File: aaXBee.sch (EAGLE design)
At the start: 67 parts, among them Q1 IRLML6244TR, U1 MCP1640C, U2 ATmega328P-AU, U3 DS3232, X1 XB24-Z7WIT-004, Y2 8MHz

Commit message: First reasonably complete routing.
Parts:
- removed C10: 27pF, _jc:C-USM0805
- removed D2: Green, adafruit:LEDCHIPLED_1206
- removed JMP1: solder jumper, _jc:R-US_M0805
- removed JP4: RTC BACKUP, SparkFun:M03LOCK
- removed R8: 1K, _jc:R-US_M0805
- removed S1: RESET, _jc:SPST-NO-MCTACT-6X3.5-SMT
- removed U3: DS3232, _jc:DS323220
- removed X1: XB24-Z7WIT-004, _jc:ULINK_XBEEOVALPADS
- removed Y2: 8MHz, _jc:CRYSTALABM2
- added A1: XB24-Z7WIT-004, _jc:ULINK_XBEEOVALPADS
- added B2: 2xAA, _jc:BATTERY-2AANOHOLES
- added C12, C13: 100nF, _jc:C-USM0805
- added C14, C16: 27pF, _jc:C-USM0805
- added L2: 10uH, _jc:INDUCTORM0805
- added L3: 4.7uH, _jc:INDUCTORNRS4018
- added PR14, PR15, PR16, PR17: PROTO-10, _jc:PROTO-10
- added R16: 562K, _jc:R-US_M0805
- added R17: 249K, _jc:R-US_M0805
- added SJ1: 5V, jumper:SJ
- added SJ2: (no value), jumper:SJ2W
- added SJ3: 3V3, jumper:SJ
- added SW1: (no value), _jc:SPST-NO-MCTACT-6X3.5-SMT
- added SW2: RESET, _jc:SPST-NO-MCTACT-6X3.5-SMT
- added U4: ATmega328P-AU, atmel:MEGA8-AI
- added U5: MCP9808, _jc:MCP9808
- added U6: DS3231, _jc:DS3231
- added Y1: 8MHz, _jc:CRYSTALABM2
- C15: value 10uF -> 100nF; device _jc:C-USC0805 -> _jc:C-USM0805
- C6, C7: value 100nF -> 10uF
- C9: value 27pF -> 100nF
- D1: value Red -> Yellow; device adafruit:LEDCHIPLED_1206 -> _jc:LEDD0805
- D7, D8: device adafruit:LEDCHIPLED_0805 -> _jc:LEDD0805
- R13, R14, R15: device _jc:R-US_R0805 -> _jc:R-US_M0805
- R3: value 249K -> 976K
- U1: value MCP1640C -> MCP1640D
- U2: value ATmega328P-AU -> MCP1640D; device atmel:MEGA8-AI -> _jc:MCP1640
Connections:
- removed net LED2: R8.2, U2.PB0(ICP)
- removed net N$11: C10.1, U2.PB7(XTAL2/TOSC2), Y2.1
- removed net N$3: D2.A, R8.1
- removed net N$39: R14.2, X1.PWM0/RSSI
- removed net N$40: R15.2, X1.ASC/AD5/DIO5
- new net AREF: C13.1, JP1.1, U4.AREF
- new net ASC: A1.ASC/AD5/DIO5, R15.2
- new net CTS: A1.CTS/DIO7, U4.PD5(T1)
- new net N$43: C14.1, U4.PB6(XTAL1/TOSC1), Y1.2
- new net N$44: C16.1, U4.PB7(XTAL2/TOSC2), Y1.1
- new net N$46: C12.1, L2.2, U4.AVCC
- new net RSSI: A1.PWM0/RSSI, R14.2
- new net SLP: A1.DTR/DI8, U4.PD6(AIN0)
- new net SW1: SW1.P$1, U4.PB0(ICP)
- net +3V3: now also C7.1, R3.1, SJ2.1, U2.VOUT; no longer C15.1, R13.1, X1.+3V3
- net /RESET: now also SW2.P$1, U4.PC6(/RESET); no longer S1.P$1, U2.PC6(/RESET)
- net /SS: now also JP1.12, U4.PB2(SS/OC1B); no longer JP1.9, U2.PB2(SS/OC1B)
- net 32KHZ: now also U6.32KHZ; no longer JP1.1, U3.32KHZ
- net ADC0: now also U4.PC0(ADC0); no longer U2.PC0(ADC0)
- net ADC1: now also U4.PC1(ADC1); no longer U2.PC1(ADC1)
- net ADC2: now also U4.PC2(ADC2); no longer U2.PC2(ADC2)
- net ADC3: now also U4.PC3(ADC3); no longer U2.PC3(ADC3)
- net ADC6: now also U4.ADC6; no longer U2.ADC6
- net ADC7: now also U4.ADC7; no longer U2.ADC7
- net BAT: now also B2.POS, C6.1, L3.1, U2.VIN; no longer JP4.1
- net EN: now also U2.EN, U4.PD4(XCK/T0); no longer U2.PD4(XCK/T0)
- net GND: now also A1.GND, B2.NEG, C12.2, C13.2, C14.2, C16.2, R16.2, R17.2, SJ1.2, SW1.P$2, SW2.P$2, U4.GND, U4.GND@1, U4.GND@2, U5.A0, U5.A1, U5.A2, U5.GND, U6.GND, U6.NC10, U6.NC11, U6.NC12, U6.NC5, U6.NC6, U6.NC7, U6.NC8, U6.NC9; no longer C10.2, D2.C, JMP1.2, R3.2, S1.P$2, U2.GND@1, U2.GND@2, U3.GND, U3.NC1, U3.NC10, U3.NC11, U3.NC12, U3.NC13, U3.NC14, U3.NC19, U3.NC2, U3.NC7, U3.NC8, U3.NC9, X1.GND
- net INT: now also U4.PD3(INT1), U6./INT-SQW; no longer U2.PD3(INT1), U3./INT-SQW
- net LED1: now also U4.PD7(AIN1); no longer U2.PD7(AIN1)
- net MISO: now also JP1.10, U4.PB4(MISO); no longer JP1.11, U2.PB4(MISO)
- net MOSI: now also JP1.11, U4.PB3(MOSI/OC2); no longer JP1.12, U2.PB3(MOSI/OC2)
- net N$1: now also U6.VBAT; no longer JP4.3
- net N$12: now also R16.1, R3.2, U2.VFB; no longer JMP1.1, R2.2, R3.1
- net N$13: now also L3.2, U2.SW; no longer C8.1, U2.AREF
- net N$35: now also A1.+3V3, C15.1, C3.1, R13.1, SJ2.2; no longer JP4.2, U3.VBAT
- net N$37: now also A1.DIN, SJ3.1; no longer X1.DIN
- net N$38: now also A1.DOUT; no longer X1.DOUT
- net N$8: now also R17.1, R2.2, SJ1.1; no longer C9.1, U2.PB6(XTAL1/TOSC1), Y2.2
- net PPWR: now also C9.1, U4.PD2(INT0), U5.VCC, U6.VCC; no longer U2.PD2(INT0), U3.VCC
- net RXD: now also U4.PD0(RXD); no longer U2.PD0(RXD)
- net SCK: now also JP1.9, U4.PB5(SCK); no longer JP1.10, U2.PB5(SCK)
- net SCL: now also R10.2, U4.PC5(ADC5/SCL), U5.SCL, U6.SCL; no longer R10.1, U2.PC5(ADC5/SCL), U3.SCL18
- net SDA: now also R9.2, U4.PC4(ADC4/SDA), U5.SDA, U6.SDA; no longer R9.1, U2.PC4(ADC4/SDA), U3.SDA
- net SPWR: now also U4.PB1(OC1A); no longer U2.PB1(OC1A)
- net TXD: now also SJ3.2, U4.PD1(TXD); no longer U2.PD1(TXD)
- net VCC: now also C8.1, L2.1, R10.1, R9.1, SJ2.3, U4.VCC@1, U4.VCC@2; no longer C3.1, C6.1, C7.1, R10.2, R9.2, U2.AVCC, U2.VCC@1, U2.VCC@2
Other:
- note added: "*Verify XBee connections!"
- note added: "Double-A XBee Sensor Node by Jack Christensen is licensed under"
- note added: "Main 5V or 3.3V supply"
- note added: "XBee 3.3V supply"
- note removed: "Double-A XBee Node by Jack Christensen is licensed under"
- moved on the sheet: B1, C1, C11, C15, C2, C3, C4, C5, C6, C7, C8, C9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

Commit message: Routing complete.
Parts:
- removed JP1: PROTO-12NR, _jc:PROTO-12NR
- removed U$1, U$2: PROTO-12PROTO, _jc:PROTO-12PROTO
- added PR18, PR19: (no value), _jc:PROTO-16
- added PR20: (no value), _jc:PROTO-14NR
- added SJ4: 5V, jumper:SJ
- SJ3: value 3V3 -> /5V
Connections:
- net +3V3 renamed N$39
- net N$35 renamed XBEE_SUPPLY
- removed net LED1: R7.2, U4.PD7(AIN1)
- removed net SW1: SW1.P$1, U4.PB0(ICP)
- new net N$35: C6.1, L3.1, SJ4.2, U2.VIN
- new net N$40: PR14.1, PR14.2, PR14.3, PR14.4, PR14.5
- new net N$45: PR14.10, PR14.6, PR14.7, PR14.8, PR14.9
- new net N$47: PR15.1, PR15.2, PR15.3, PR15.4, PR15.5
- new net N$48: PR15.10, PR15.6, PR15.7, PR15.8, PR15.9
- new net N$49: PR16.1, PR16.2, PR16.3, PR16.4, PR16.5
- new net N$50: PR16.10, PR16.6, PR16.7, PR16.8, PR16.9
- new net N$51: PR17.1, PR17.2, PR17.3, PR17.4, PR17.5
- new net N$52: PR17.10, PR17.6, PR17.7, PR17.8, PR17.9
- new net PB0: R7.2, U4.PB0(ICP)
- new net PD7: SW1.P$1, U4.PD7(AIN1)
- net /SS: now also PR20.3; no longer JP1.12
- net ADC0: now also PR20.9; no longer JP1.7
- net ADC1: now also PR20.10; no longer JP1.6
- net ADC2: now also PR20.11; no longer JP1.5
- net ADC3: now also PR20.12; no longer JP1.4
- net ADC6: now also PR20.7; no longer JP1.8
- net AREF: now also PR20.8; no longer JP1.1
- net BAT: now also SJ4.1; no longer C6.1, L3.1, U2.VIN
- net MISO: now also PR20.5; no longer JP1.10
- net MOSI: now also PR20.4; no longer JP1.11
- net SCK: now also PR20.6; no longer JP1.9
- net SCL: now also PR20.14; no longer JP1.2
- net SDA: now also PR20.13; no longer JP1.3
- net SGND: now also PR18.1, PR18.10, PR18.11, PR18.12, PR18.13, PR18.14, PR18.15, PR18.16, PR18.2, PR18.3, PR18.4, PR18.5, PR18.6, PR18.7, PR18.8, PR18.9; no longer U$2.1, U$2.10, U$2.11, U$2.12, U$2.2, U$2.3, U$2.4, U$2.5, U$2.6, U$2.7, U$2.8, U$2.9
- net VCC: now also PR19.1, PR19.10, PR19.11, PR19.12, PR19.13, PR19.14, PR19.15, PR19.16, PR19.2, PR19.3, PR19.4, PR19.5, PR19.6, PR19.7, PR19.8, PR19.9; no longer U$1.1, U$1.10, U$1.11, U$1.12, U$1.2, U$1.3, U$1.4, U$1.5, U$1.6, U$1.7, U$1.8, U$1.9
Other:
- moved on the sheet: JP3, Q1, R11, R12, SJ2

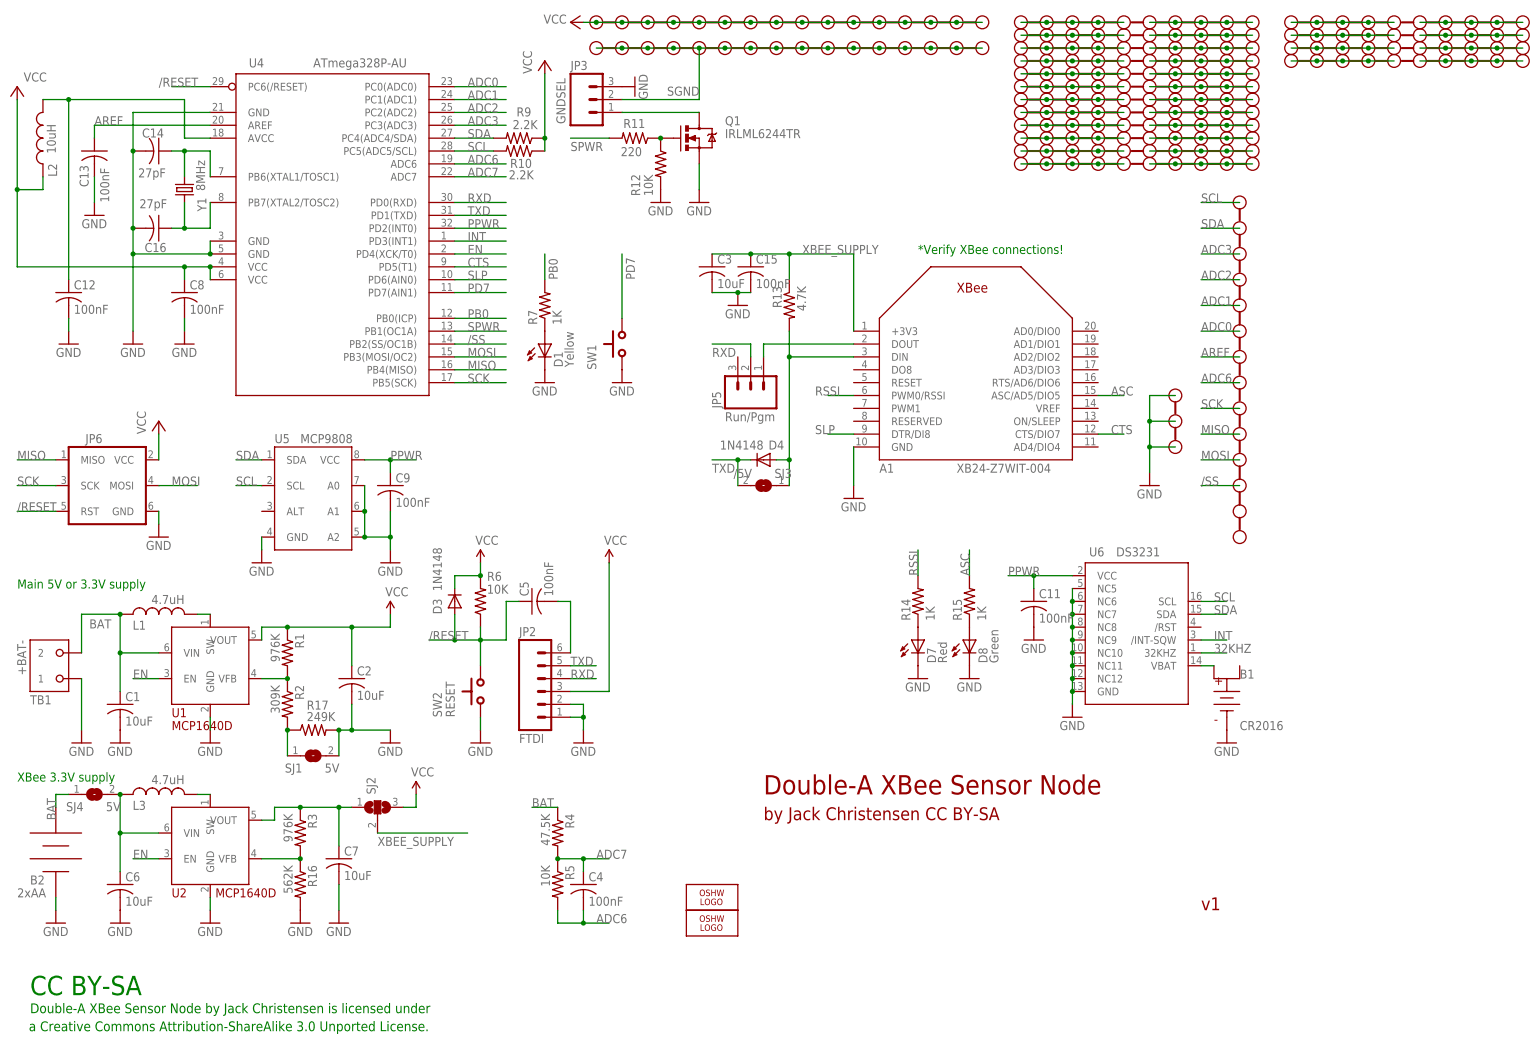
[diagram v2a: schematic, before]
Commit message: Tweak a few traces.
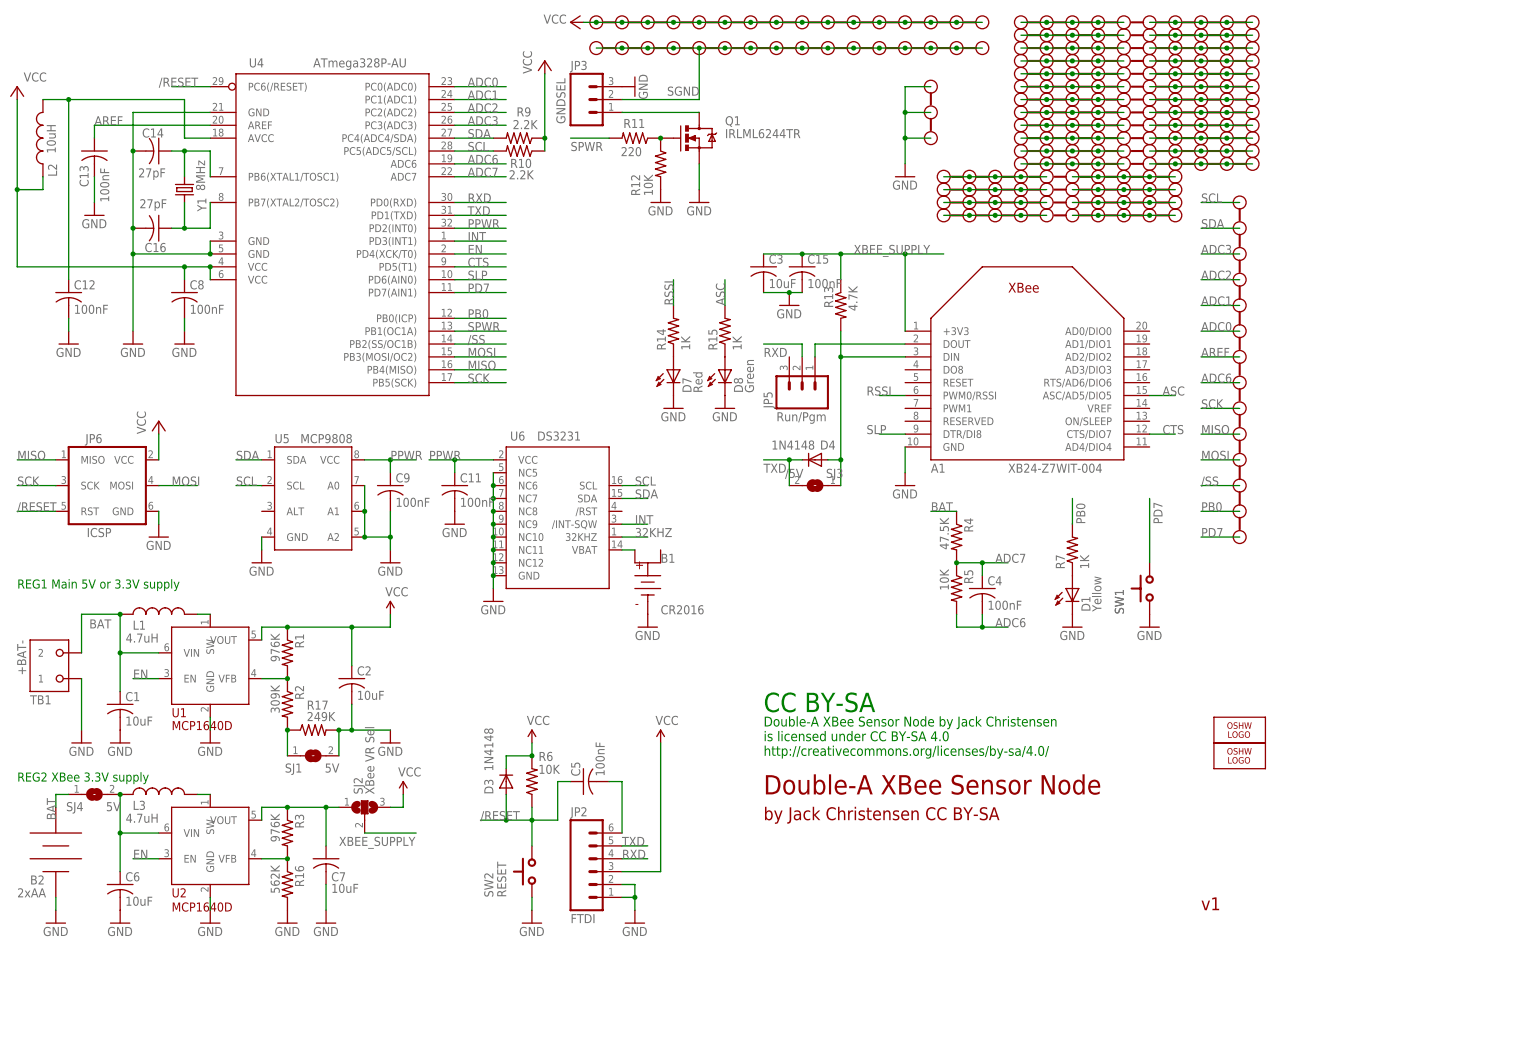
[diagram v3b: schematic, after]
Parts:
- D1, D7: device _jc:LEDD0805 -> _jc:LEDD0805A
- JP6: value (none) -> ICSP
- PR18: value (none) -> Proto ground
- PR19: value (none) -> Proto Vcc
- PR20: value (none) -> Signals
- SJ2: value (none) -> XBee VR Sel
- SW1: value (none) -> SW1
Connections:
- net PB0: now also PR20.2
- net PD7: now also PR20.1
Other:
- note added: "Double-A XBee Sensor Node by Jack Christensen is licensed under CC BY-SA 4.0 http://creativecommons.org/licenses/by-sa/4.0/"
- note added: "REG1 Main 5V or 3.3V supply"
- note added: "REG2 XBee 3.3V supply"
- note removed: "*Verify XBee connections!"
- note removed: "Double-A XBee Sensor Node by Jack Christensen is licensed under"
- note removed: "Main 5V or 3.3V supply"
- note removed: "XBee 3.3V supply"
- note removed: "a Creative Commons Attribution-ShareAlike 3.0 Unported License."
- moved on the sheet: A1, B1, C11, C15, C3, C4, C5, C7, D1, D3, D4, D7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

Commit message: Rename some components to be sequential. Cosmetic adjustments to schematic.
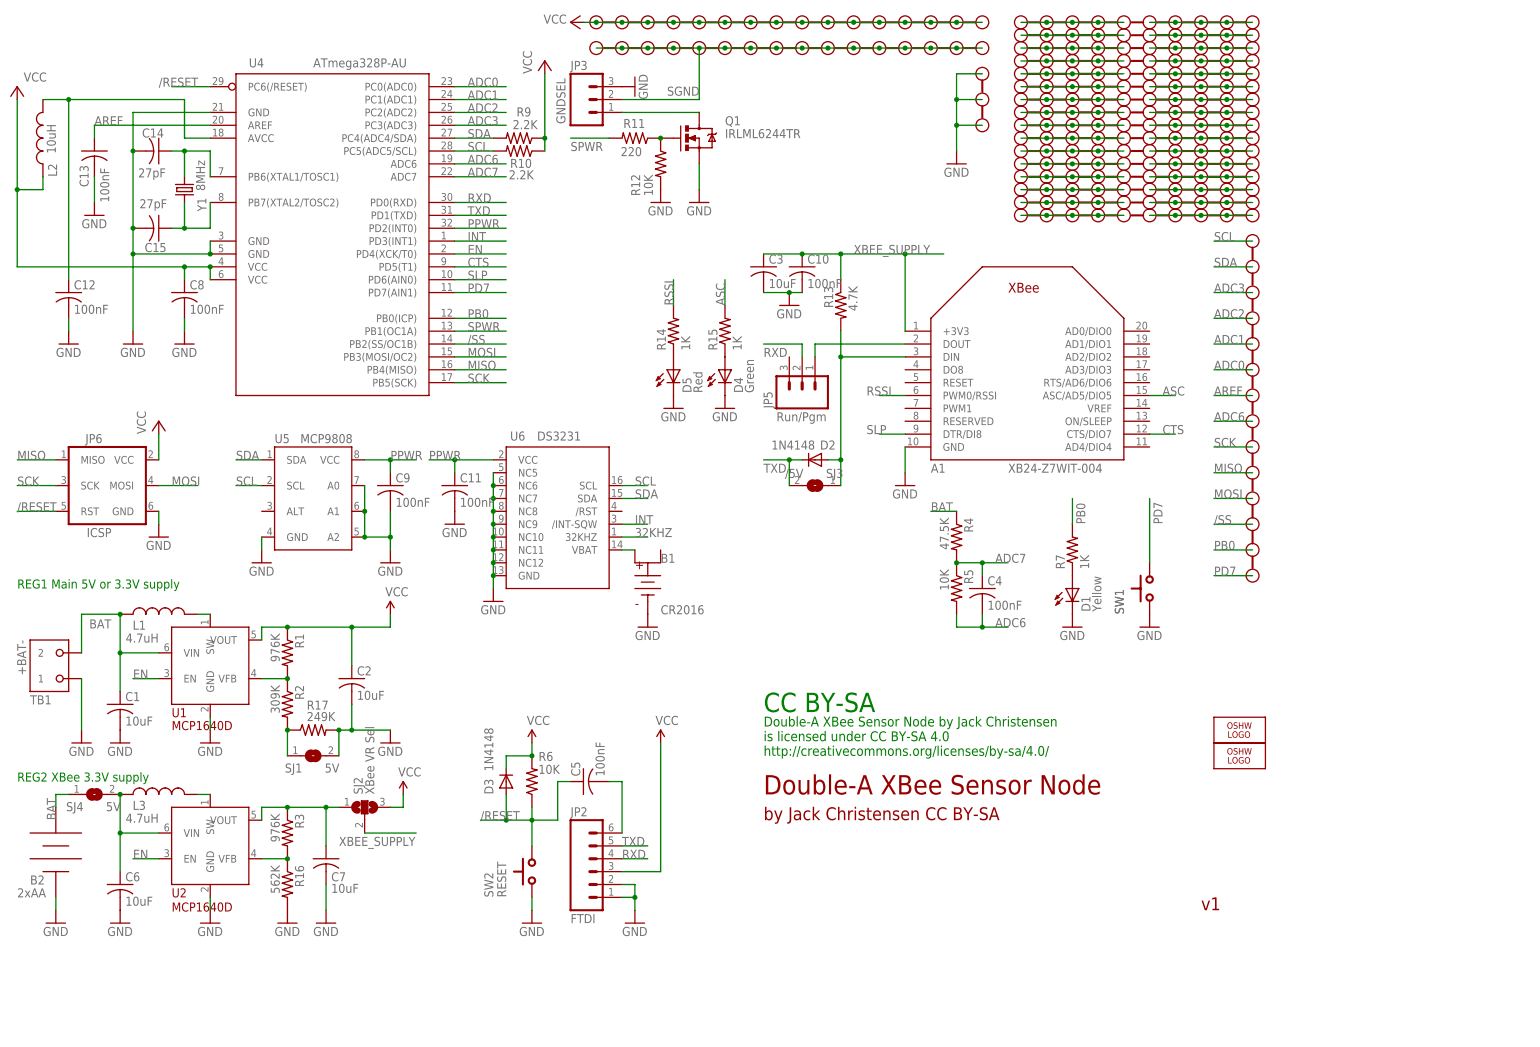
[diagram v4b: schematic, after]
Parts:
- removed C16: 27pF, _jc:C-USM0805
- removed D8: Green, _jc:LEDD0805
- added C10: 100nF, _jc:C-USM0805
- added D2: 1N4148, _jc:DIODESOD-323F
- C15: value 100nF -> 27pF
- D4: value 1N4148 -> Green; device _jc:DIODESOD-323F -> _jc:LEDD0805
- renumbered D7 to D5
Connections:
- net GND: now also C10.2, D4.C; no longer C16.2, D8.C
- net N$37: now also D2.A; no longer D4.A
- net N$42: now also D4.A; no longer D8.A
- net N$44: now also C15.1; no longer C16.1
- net TXD: now also D2.K; no longer D4.K
- net XBEE_SUPPLY: now also C10.1; no longer C15.1
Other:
- moved on the sheet: C15
